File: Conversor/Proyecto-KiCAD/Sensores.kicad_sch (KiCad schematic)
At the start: 26 parts, among them U10 OPA365xxD, U7 TMCS1100A4, U8 LM5056APMH/NOPB, U9 ISO7242C

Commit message: Comenzar a asignar footprints a todos los componentes
- Agregado un header para conectar el módulo de tarjeta SD de Arduino
por SPI
- Los GNDs conectados por resistencias nulas son para conectar los GNDs
en caso de que fuera necesario
- Agregar una nota de aplicaión de aislación para I2C (creo que como
estan conectados SDAO y SDAI está bien)
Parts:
- C18, C19, C20, C21, C22, C23, C24, C25, C26, C27: footprint (none) -> Capacitor_SMD:C_1206_3216Metric_Pad1.33x1.80mm_HandSolder
- R11, R12, R13, R14, R16, R18, R19, R20, R8, R9: footprint (none) -> Resistor_SMD:R_1206_3216Metric_Pad1.30x1.75mm_HandSolder
- U7: footprint (none) -> Package_SO:SOIC-8_3.9x4.9mm_P1.27mm
- U8: footprint PWP28_TEX -> Package_SO:HTSSOP-28-1EP_4.4x9.7mm_P0.65mm_EP2.85x5.4mm
- U9: footprint (none) -> Package_SO:SOIC-16W_7.5x10.3mm_P1.27mm
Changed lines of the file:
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@@
     (property "Reference" "R20" (id 0) (at 67.31 125.73 90))
     (property "Value" "R" (id 1) (at 67.31 130.81 90))
-    (property "Footprint" "" (id 2) (at 67.31 128.27 0)
+    (property "Footprint" "Resistor_SMD:R_1206_3216Metric_Pad1.30x1.75mm_HandSolder" (id 2) (at 67.31 128.27 0)
       (effects (font (size 1.27 1.27)) hide)
     )
@@
       (effects (font (size 1.27 1.27)) (justify left))
     )
-    (property "Footprint" "" (id 2) (at 149.606 48.514 90)
+    (property "Footprint" "Resistor_SMD:R_1206_3216Metric_Pad1.30x1.75mm_HandSolder" (id 2) (at 149.606 48.514 90)
       (effects (font (size 1.27 1.27)) hide)
     )
@@
       (effects (font (size 1.27 1.27)) (justify left))
     )
-    (property "Footprint" "" (id 2) (at 143.256 48.514 90)
+    (property "Footprint" "Resistor_SMD:R_1206_3216Metric_Pad1.30x1.75mm_HandSolder" (id 2) (at 143.256 48.514 90)
       (effects (font (size 1.27 1.27)) hide)
     )
@@
     (property "Reference" "U7" (id 0) (at 226.06 125.73 0))
     (property "Value" "TMCS1100A4" (id 1) (at 226.06 128.27 0))
-    (property "Footprint" "" (id 2) (at 226.06 144.78 0)
+    (property "Footprint" "Package_SO:SOIC-8_3.9x4.9mm_P1.27mm" (id 2) (at 226.06 144.78 0)
       (effects (font (size 1.27 1.27)) hide)
     )
@@
       (effects (font (size 1.27 1.27)) (justify left))
     )
-    (property "Footprint" "" (id 2) (at 99.06 114.3 0)
+    (property "Footprint" "Capacitor_SMD:C_1206_3216Metric_Pad1.33x1.80mm_HandSolder" (id 2) (at 99.06 114.3 0)
       (effects (font (size 1.27 1.27)) hide)
     )
@@
     (property "Reference" "R13" (id 0) (at 113.03 120.65 90))
     (property "Value" "R3amp" (id 1) (at 113.03 123.19 90))
-    (property "Footprint" "" (id 2) (at 112.776 124.714 90)
+    (property "Footprint" "Resistor_SMD:R_1206_3216Metric_Pad1.30x1.75mm_HandSolder" (id 2) (at 112.776 124.714 90)
       (effects (font (size 1.27 1.27)) hide)
     )
@@
       (effects (font (size 1.27 1.27)) (justify right))
     )
-    (property "Footprint" "" (id 2) (at 124.46 31.75 0)
+    (property "Footprint" "Capacitor_SMD:C_1206_3216Metric_Pad1.33x1.80mm_HandSolder" (id 2) (at 124.46 31.75 0)
       (effects (font (size 1.27 1.27)) hide)
     )
@@
     (property "Reference" "U9" (id 0) (at 116.84 46.99 0))
     (property "Value" "ISO7242C" (id 1) (at 116.84 49.53 0))
-    (property "Footprint" "" (id 2) (at 116.84 63.5 0)
+    (property "Footprint" "Package_SO:SOIC-16W_7.5x10.3mm_P1.27mm" (id 2) (at 116.84 63.5 0)
       (effects (font (size 1.27 1.27)) hide)
     )
@@
       (effects (font (size 1.27 1.27)) (justify left))
     )
-    (property "Footprint" "" (id 2) (at 189.23 50.8 0)
+    (property "Footprint" "Capacitor_SMD:C_1206_3216Metric_Pad1.33x1.80mm_HandSolder" (id 2) (at 189.23 50.8 0)
       (effects (font (size 1.27 1.27)) hide)
     )
@@
       (effects (font (size 1.524 1.524)))
     )
-    (property "Footprint" "PWP28_TEX" (id 2) (at 184.15 30.734 0)
+    (property "Footprint" "Package_SO:HTSSOP-28-1EP_4.4x9.7mm_P0.65mm_EP2.85x5.4mm" (id 2) (at 184.15 30.734 0)
       (effects (font (size 1.524 1.524)) hide)
     )
@@
       (effects (font (size 1.27 1.27)) (justify left))
     )
-    (property "Footprint" "" (id 2) (at 91.186 48.514 90)
+    (property "Footprint" "Resistor_SMD:R_1206_3216Metric_Pad1.30x1.75mm_HandSolder" (id 2) (at 91.186 48.514 90)
       (effects (font (size 1.27 1.27)) hide)
     )
@@
       (effects (font (size 1.27 1.27)) (justify left))
     )
-    (property "Footprint" "" (id 2) (at 57.15 134.62 0)
+    (property "Footprint" "Capacitor_SMD:C_1206_3216Metric_Pad1.33x1.80mm_HandSolder" (id 2) (at 57.15 134.62 0)
       (effects (font (size 1.27 1.27)) hide)
     )
@@
       (effects (font (size 1.27 1.27)) (justify left))
     )
-    (property "Footprint" "" (id 2) (at 105.156 114.046 90)
+    (property "Footprint" "Resistor_SMD:R_1206_3216Metric_Pad1.30x1.75mm_HandSolder" (id 2) (at 105.156 114.046 90)
       (effects (font (size 1.27 1.27)) hide)
     )
@@
     (property "Reference" "R12" (id 0) (at 113.03 133.35 90))
     (property "Value" "R1amp" (id 1) (at 113.03 135.89 90))
-    (property "Footprint" "" (id 2) (at 112.776 129.794 90)
+    (property "Footprint" "Resistor_SMD:R_1206_3216Metric_Pad1.30x1.75mm_HandSolder" (id 2) (at 112.776 129.794 90)
       (effects (font (size 1.27 1.27)) hide)
     )
@@
     (property "Reference" "C25" (id 0) (at 86.36 162.56 90))
     (property "Value" "C2amp" (id 1) (at 86.36 160.02 90))
-    (property "Footprint" "" (id 2) (at 86.36 156.21 0)
+    (property "Footprint" "Capacitor_SMD:C_1206_3216Metric_Pad1.33x1.80mm_HandSolder" (id 2) (at 86.36 156.21 0)
       (effects (font (size 1.27 1.27)) hide)
     )
@@
       (effects (font (size 1.27 1.27)) (justify left))
     )
-    (property "Footprint" "" (id 2) (at 84.836 48.514 90)
+    (property "Footprint" "Resistor_SMD:R_1206_3216Metric_Pad1.30x1.75mm_HandSolder" (id 2) (at 84.836 48.514 90)
       (effects (font (size 1.27 1.27)) hide)
     )
@@
       (effects (font (size 1.27 1.27)) (justify left))
     )
-    (property "Footprint" "" (id 2) (at 109.22 31.75 0)
+    (property "Footprint" "Capacitor_SMD:C_1206_3216Metric_Pad1.33x1.80mm_HandSolder" (id 2) (at 109.22 31.75 0)
       (effects (font (size 1.27 1.27)) hide)
     )
@@
       (effects (font (size 1.27 1.27)) (justify left))
     )
-    (property "Footprint" "" (id 2) (at 155.956 48.514 90)
+    (property "Footprint" "Resistor_SMD:R_1206_3216Metric_Pad1.30x1.75mm_HandSolder" (id 2) (at 155.956 48.514 90)
       (effects (font (size 1.27 1.27)) hide)
     )
@@
     (property "Reference" "R16" (id 0) (at 86.36 146.05 90))
     (property "Value" "R2amp" (id 1) (at 86.36 143.51 90))
-    (property "Footprint" "" (id 2) (at 86.106 149.606 90)
+    (property "Footprint" "Resistor_SMD:R_1206_3216Metric_Pad1.30x1.75mm_HandSolder" (id 2) (at 86.106 149.606 90)
       (effects (font (size 1.27 1.27)) hide)
     )
@@
       (effects (font (size 1.27 1.27)) (justify left))
     )
-    (property "Footprint" "" (id 2) (at 199.39 124.46 0)
+    (property "Footprint" "Capacitor_SMD:C_1206_3216Metric_Pad1.33x1.80mm_HandSolder" (id 2) (at 199.39 124.46 0)
       (effects (font (size 1.27 1.27)) hide)
     )
@@
       (effects (font (size 1.27 1.27)) (justify left))
     )
-    (property "Footprint" "" (id 2) (at 257.81 74.93 0)
+    (property "Footprint" "Capacitor_SMD:C_1206_3216Metric_Pad1.33x1.80mm_HandSolder" (id 2) (at 257.81 74.93 0)
       (effects (font (size 1.27 1.27)) hide)
     )
@@
     (property "Reference" "C26" (id 0) (at 82.55 113.03 90))
     (property "Value" "C" (id 1) (at 82.55 118.11 90))
-    (property "Footprint" "" (id 2) (at 82.55 115.57 0)
+    (property "Footprint" "Capacitor_SMD:C_1206_3216Metric_Pad1.33x1.80mm_HandSolder" (id 2) (at 82.55 115.57 0)
       (effects (font (size 1.27 1.27)) hide)
     )
@@
       (effects (font (size 1.27 1.27)) (justify left))
     )
-    (property "Footprint" "" (id 2) (at 266.7 44.45 0)
-      (effects (font (size 1.27 1.27)) hide)
-    )
+    (property "Footprint" "Capacitor_SMD:C_1206_3216Metric_Pad1.33x1.80mm_HandSolder" (id 2) (at 266.7 44.45 0)
+      (effects (font (size 1.27 1.27)) hide)
+    )

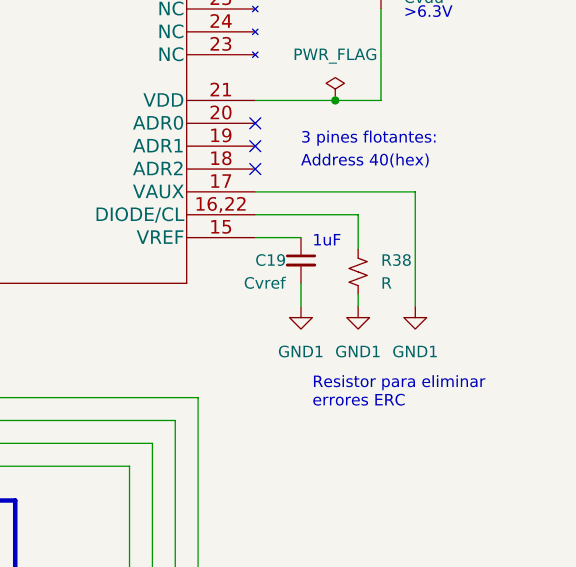
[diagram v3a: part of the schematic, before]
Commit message: Comenzar el layout de componentes de la PCB
- Todos los componentes con footprints asignados (preliminar)
- Organizados los componentes de la placa adaptadora en el esquema del
PCB (usando como guia aproximada la placa adaptadora)
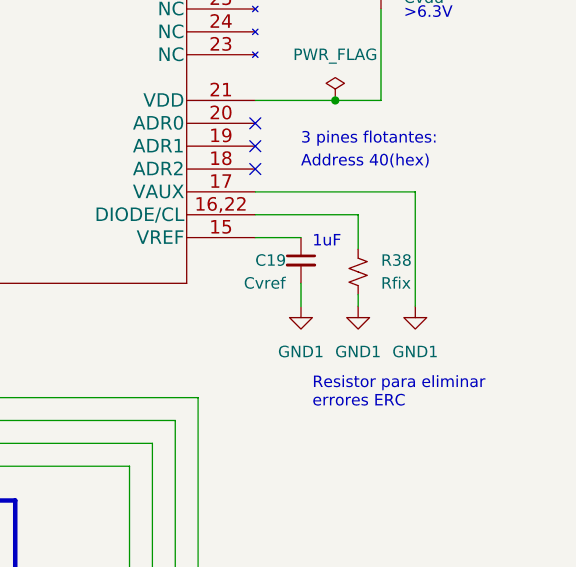
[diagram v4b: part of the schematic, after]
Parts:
- R38: value R -> Rfix; footprint (none) -> Resistor_SMD:R_1206_3216Metric_Pad1.30x1.75mm_HandSolder
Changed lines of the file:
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@@
       (effects (font (size 1.27 1.27)) (justify left))
     )
-    (property "Value" "R" (id 1) (at 266.7 77.4699 0)
+    (property "Value" "Rfix" (id 1) (at 266.7 77.4699 0)
       (effects (font (size 1.27 1.27)) (justify left))
     )
-    (property "Footprint" "" (id 2) (at 264.16 76.2 0)
+    (property "Footprint" "Resistor_SMD:R_1206_3216Metric_Pad1.30x1.75mm_HandSolder" (id 2) (at 264.16 76.2 0)
       (effects (font (size 1.27 1.27)) hide)
     )

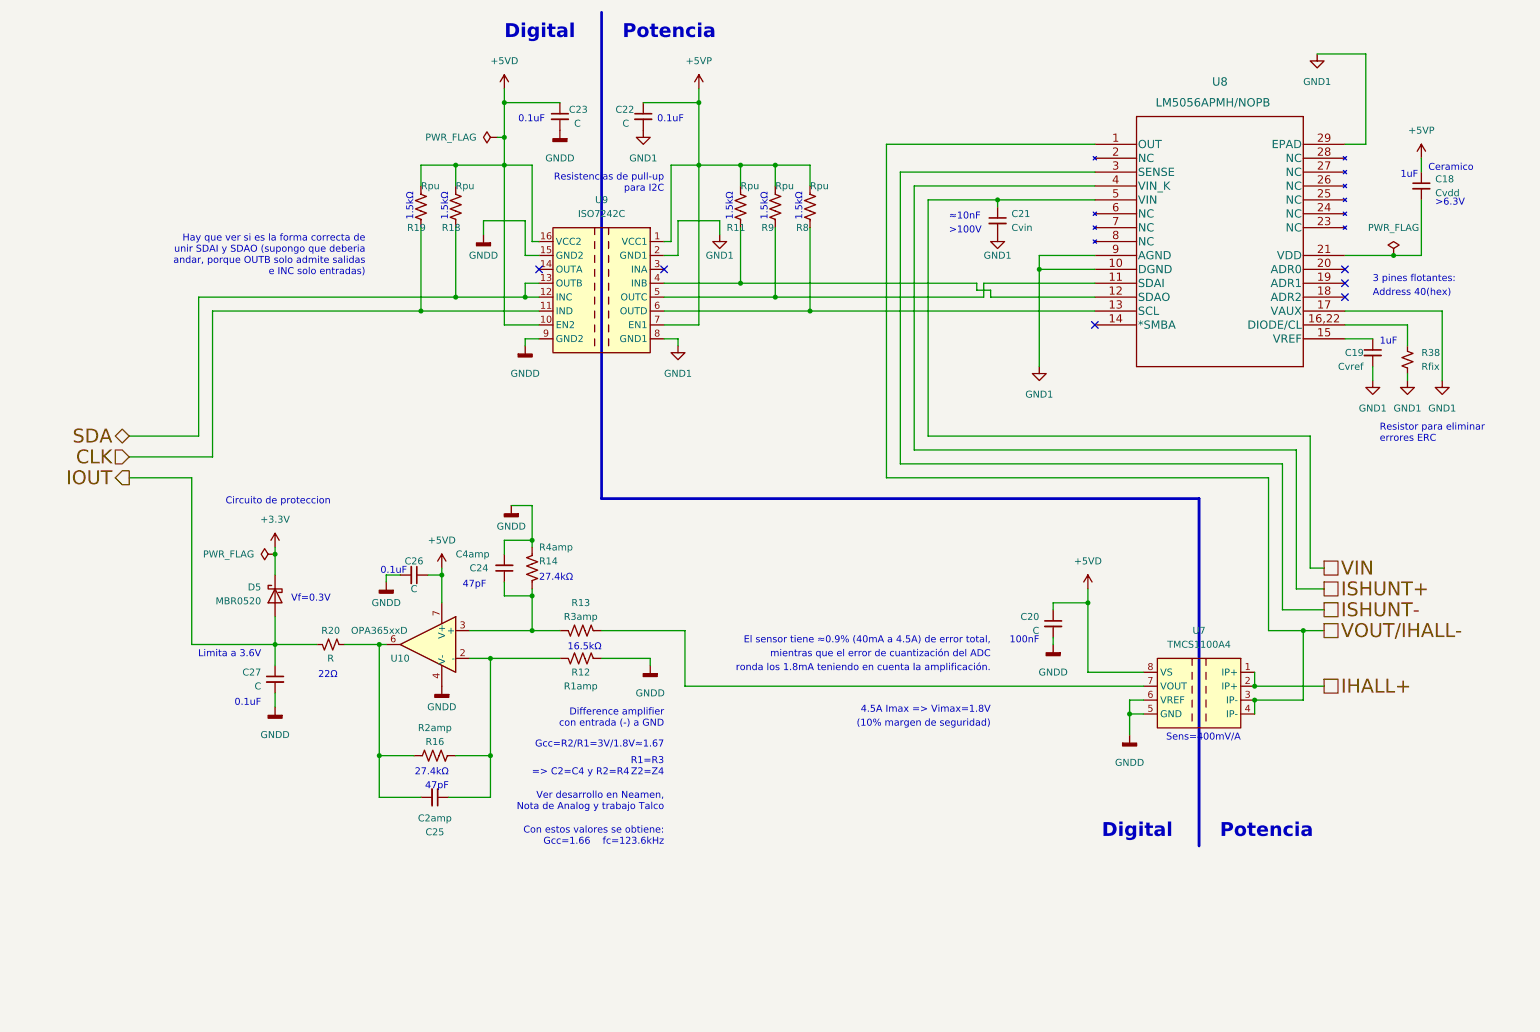
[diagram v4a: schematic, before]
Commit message: Reempezar el ordenado de componentes del PCB
- Intentar copiar mas a la placa adaptadora en la parte del DSP (digital)
  - Algunas cosas (como los headers y la parte de USB) se movieron para hacer entrar mejor las cosas
- Layout bastante completo
- Agregados algunos modelos 3D faltantes
Por hacer:
  - Mover y reorganizar la parte del LM5056, porque tiene una pata que va al secundario, y ahora esta muy lejos del area de GND2
  - Ver como reorganizar un poco para que no queden esquinas vacias
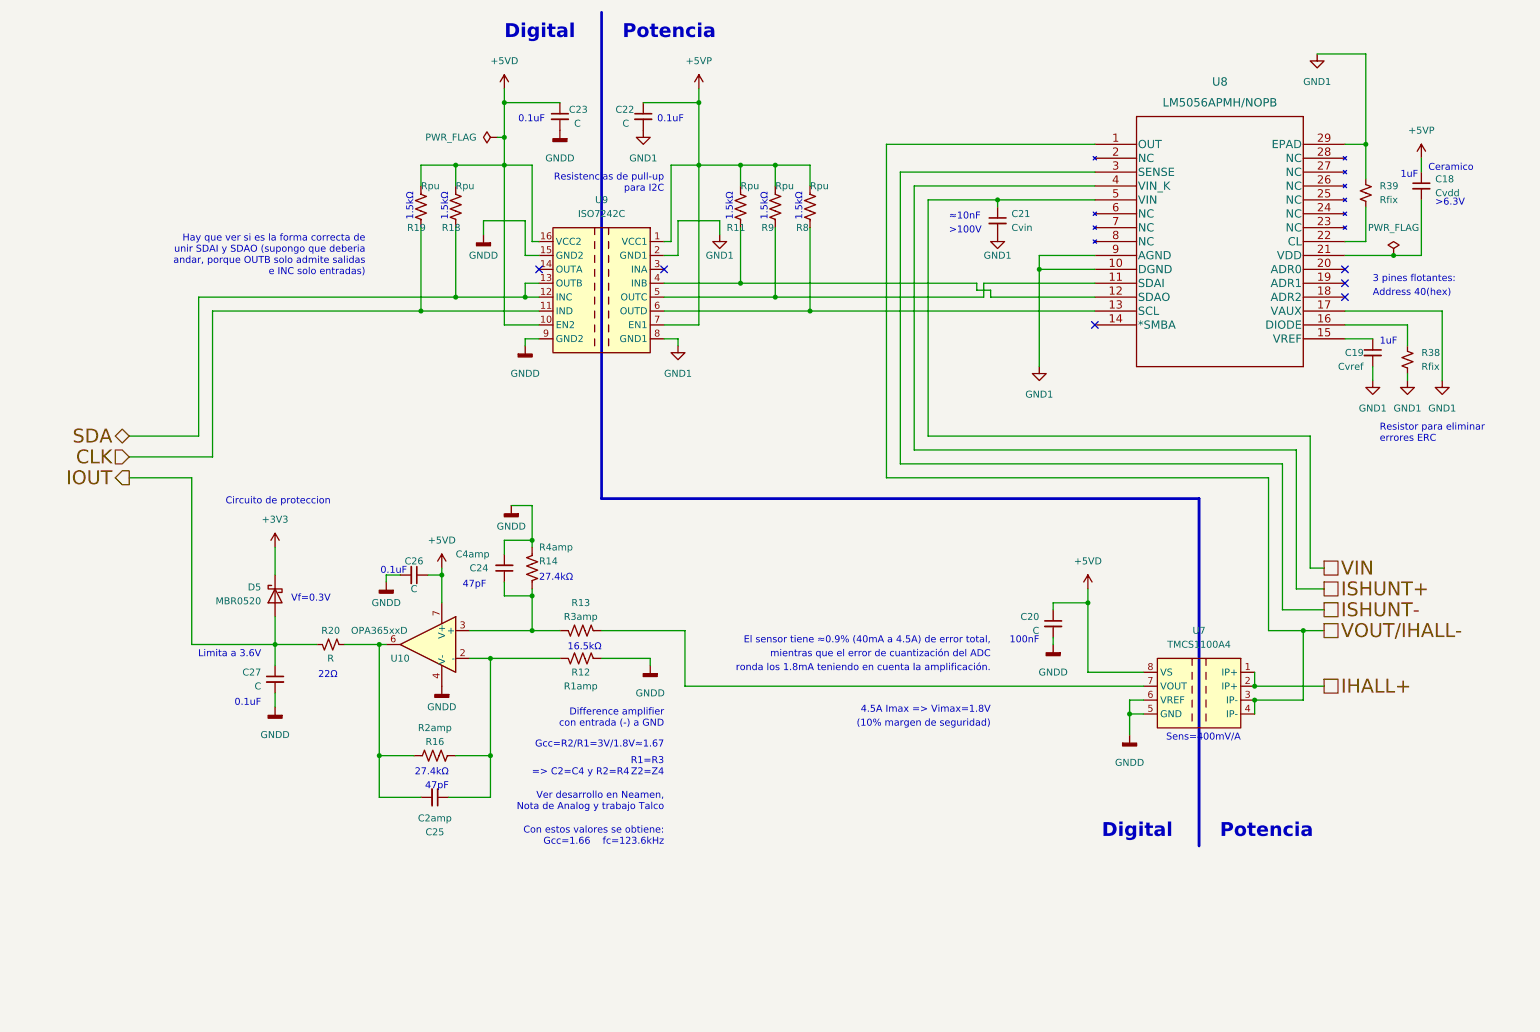
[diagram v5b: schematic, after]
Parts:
- added R39: Rfix, Resistor_SMD:R_1206_3216Metric_Pad1.30x1.75mm_HandSolder, symbol Device:R_Small_US
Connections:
- net GND1: now also R39.1
- net at R38.1: now also U8.16 (DIODE); no longer U8.16,22 (DIODE/CL)
- new net: R39.2, U8.22 (CL)

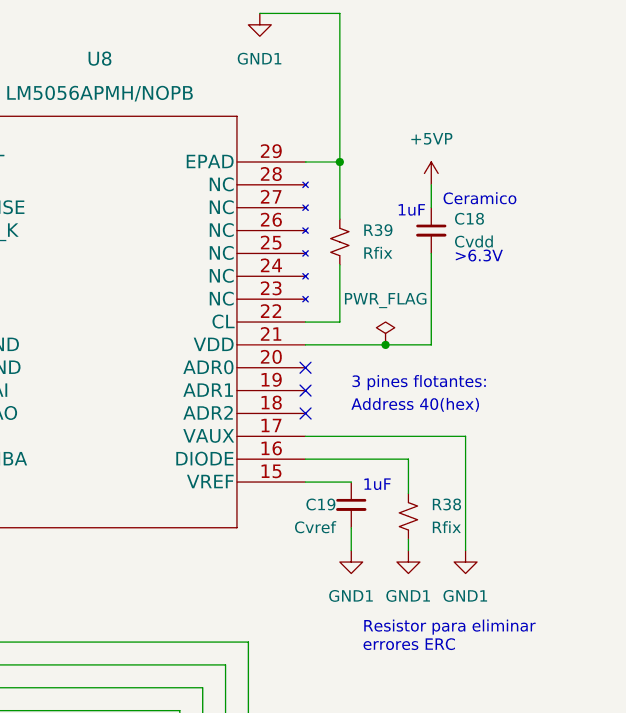
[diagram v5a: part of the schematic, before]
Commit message: Terminar la parte digital de la PCB (incluidas las pistas)
- Hay que ver si la clearance de 0.254mm para el plano de GNDD esta bien
- Cambiar la footprint del FTDI por la version correcta
- Borrar R37, R38 y R39 (usadas para corregir errores del ERC)
Por hacer:
  - Terminar las otras dos partes de la placa
  - Consultar si esta bien lo que hice hasta ahora
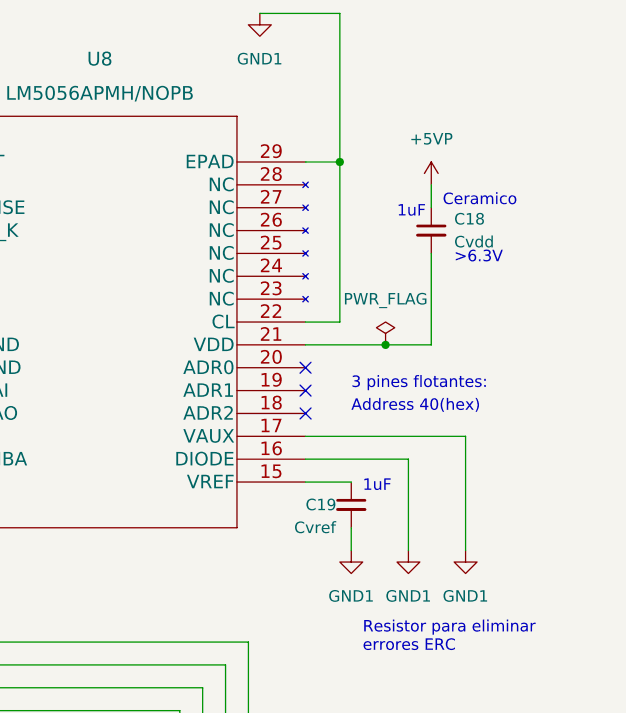
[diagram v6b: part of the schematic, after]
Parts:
- removed R38, R39: Rfix, Resistor_SMD:R_1206_3216Metric_Pad1.30x1.75mm_HandSolder, symbol Device:R_Small_US
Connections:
- net GND1: now also U8.16 (DIODE), U8.22 (CL)
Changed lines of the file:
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@@
     (stroke (width 0) (type default) (color 0 0 0 0))
   )
-  (wire (pts (xy 264.16 73.66) (xy 264.16 69.85))
+  (wire (pts (xy 264.16 69.85) (xy 264.16 80.01))
     (stroke (width 0) (type default) (color 0 0 0 0))
   )
@@
   )
   (wire (pts (xy 252.73 54.61) (xy 256.54 54.61))
-    (stroke (width 0) (type default) (color 0 0 0 0))
-  )
-  (wire (pts (xy 264.16 80.01) (xy 264.16 78.74))
     (stroke (width 0) (type default) (color 0 0 0 0))
   )
@@
     (stroke (width 0) (type default) (color 0 0 0 0))
   )
-  (wire (pts (xy 256.54 48.26) (xy 256.54 54.61))
-    (stroke (width 0) (type default) (color 0 0 0 0))
-  )
   (wire (pts (xy 41.91 128.27) (xy 41.91 97.79))
     (stroke (width 0) (type default) (color 0 0 0 0))
@@
     (stroke (width 0) (type default) (color 0 0 0 0))
   )
-  (wire (pts (xy 256.54 36.83) (xy 256.54 43.18))
+  (wire (pts (xy 256.54 36.83) (xy 256.54 54.61))
     (stroke (width 0) (type default) (color 0 0 0 0))
   )
@@
     (pin "1")
   )
-  (symbol (lib_id "Device:R_Small_US") (at 256.54 45.72 0) (unit 1)
-    (in_bom yes) (on_board yes) (fields_autoplaced)
-    (property "Reference" "R39" (id 0) (at 259.08 44.4499 0)
-      (effects (font (size 1.27 1.27)) (justify left))
-    )
-    (property "Value" "Rfix" (id 1) (at 259.08 46.9899 0)
-      (effects (font (size 1.27 1.27)) (justify left))
-    )
-    (property "Footprint" "Resistor_SMD:R_1206_3216Metric_Pad1.30x1.75mm_HandSolder" (id 2) (at 256.54 45.72 0)
-      (effects (font (size 1.27 1.27)) hide)
-    )
-    (property "Datasheet" "~" (id 3) (at 256.54 45.72 0)
-      (effects (font (size 1.27 1.27)) hide)
-    )
-    (pin "1")
-    (pin "2")
-  )
   (symbol (lib_id "Device:R_US") (at 90.17 48.26 0) (unit 1)
     (in_bom yes) (on_board yes)
@@
     (pin "1")
   )
-  (symbol (lib_id "Device:R_Small_US") (at 264.16 76.2 0) (unit 1)
-    (in_bom yes) (on_board yes) (fields_autoplaced)
-    (property "Reference" "R38" (id 0) (at 266.7 74.9299 0)
-      (effects (font (size 1.27 1.27)) (justify left))
-    )
-    (property "Value" "Rfix" (id 1) (at 266.7 77.4699 0)
-      (effects (font (size 1.27 1.27)) (justify left))
-    )
-    (property "Footprint" "Resistor_SMD:R_1206_3216Metric_Pad1.30x1.75mm_HandSolder" (id 2) (at 264.16 76.2 0)
-      (effects (font (size 1.27 1.27)) hide)
-    )
-    (property "Datasheet" "~" (id 3) (at 264.16 76.2 0)
-      (effects (font (size 1.27 1.27)) hide)
-    )
-    (pin "1")
-    (pin "2")
-  )
   (symbol (lib_id "Diode:MBR0520") (at 57.15 119.38 90) (mirror x) (unit 1)
